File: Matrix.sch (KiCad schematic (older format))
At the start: 180 parts

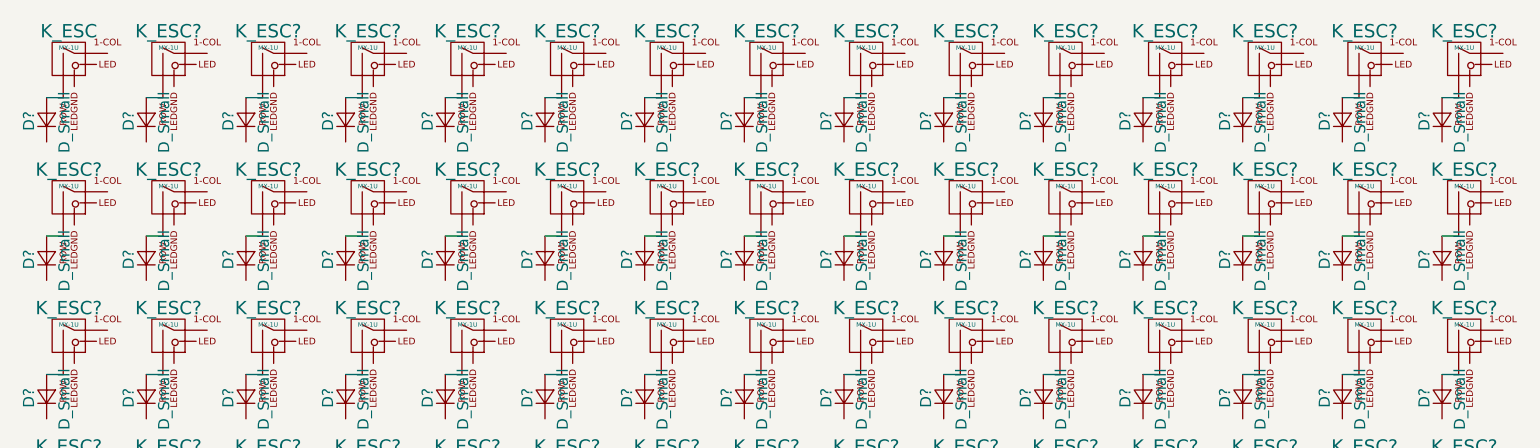
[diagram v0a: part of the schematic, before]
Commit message: Label row 1 of switches
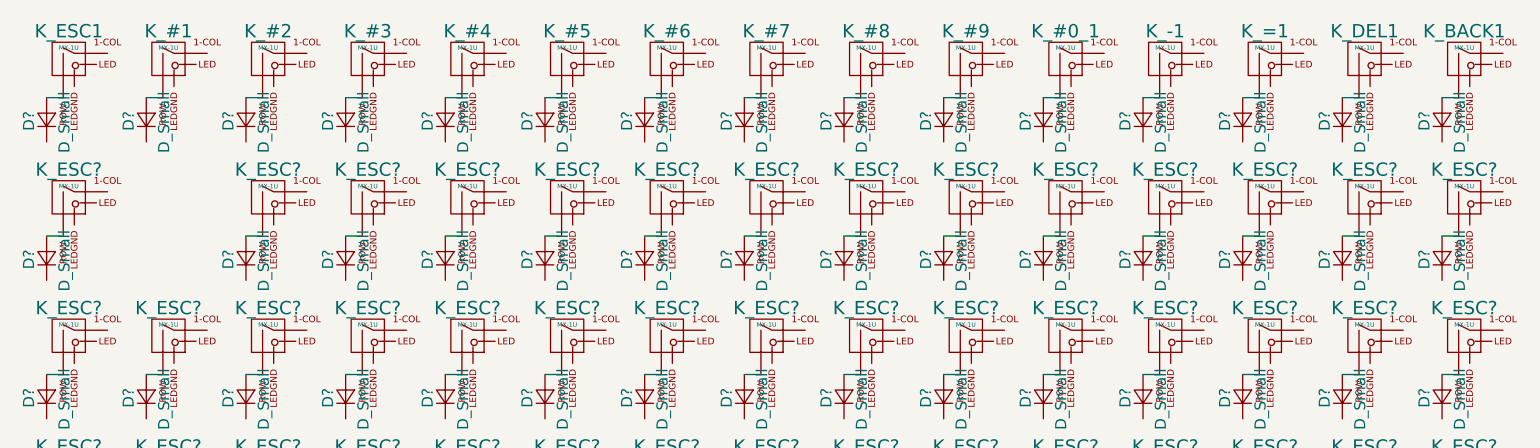
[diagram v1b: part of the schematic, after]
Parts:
- removed D?: D_Small, symbol D_Small
- removed K_ESC?: MX-1U, symbol MX-1U
- gave numbers to parts that had none: 14
- renumbered K_ESC to K_ESC1
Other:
- moved on the sheet: D?, K_#0_1, K_#1, K_#2, K_#3, K_#4, K_#5, K_#6, K_#7, K_#8, K_#9, K_-1
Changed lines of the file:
@@
 $EndDescr
 $Comp
-L MX-1U K_ESC
+L MX-1U K_ESC1
 U 1 1 5A641474
 P 1500 1225
-F 0 "K_ESC" H 1500 1350 60  0000 C CNN
+F 0 "K_ESC1" H 1500 1350 60  0000 C CNN
 F 1 "MX-1U" H 1500 1275 20  0000 C CNN
 F 2 "" H 1475 1200 60  0001 C CNN
@@
 	1475 1400 1400 1400
 $Comp
-L MX-1U K_ESC?
+L MX-1U K_-1
 U 1 1 5A646A8C
+P 6450 1225
+F 0 "K_-1" H 6450 1350 60  0000 C CNN
+F 1 "MX-1U" H 6450 1275 20  0000 C CNN
+F 2 "" H 6425 1200 60  0001 C CNN
+F 3 "" H 6425 1200 60  0001 C CNN
+	1    6450 1225
+	1    0    0    -1
+$EndComp
+$Comp
+L D_Small D?
+U 1 1 5A646A92
+P 6350 1500
+F 0 "D?" H 6300 1580 50  0000 L CNN
+F 1 "D_Small" H 6200 1420 50  0000 L CNN
+F 2 "" V 6350 1500 50  0001 C CNN
+F 3 "" V 6350 1500 50  0001 C CNN
+	1    6350 1500
+	0    -1   -1   0
+$EndComp
+Wire Wire Line
+	6425 1400 6350 1400
+$Comp
+L MX-1U K_#1
+U 1 1 5A646B3D
 P 1950 1225
-F 0 "K_ESC?" H 1950 1350 60  0000 C CNN
+F 0 "K_#1" H 1950 1350 60  0000 C CNN
 F 1 "MX-1U" H 1950 1275 20  0000 C CNN
 F 2 "" H 1925 1200 60  0001 C CNN
@@
 $Comp
 L D_Small D?
-U 1 1 5A646A92
+U 1 1 5A646B43
 P 1850 1500
 F 0 "D?" H 1800 1580 50  0000 L CNN
@@
 	1925 1400 1850 1400
 $Comp
-L MX-1U K_ESC?
-U 1 1 5A646B3D
+L MX-1U K_#2
+U 1 1 5A646B4A
 P 2400 1225
-F 0 "K_ESC?" H 2400 1350 60  0000 C CNN
+F 0 "K_#2" H 2400 1350 60  0000 C CNN
 F 1 "MX-1U" H 2400 1275 20  0000 C CNN
 F 2 "" H 2375 1200 60  0001 C CNN
@@
 $Comp
 L D_Small D?
-U 1 1 5A646B43
+U 1 1 5A646B50
 P 2300 1500
 F 0 "D?" H 2250 1580 50  0000 L CNN
@@
 	2375 1400 2300 1400
 $Comp
-L MX-1U K_ESC?
-U 1 1 5A646B4A
+L MX-1U K_#3
+U 1 1 5A646D37
 P 2850 1225
-F 0 "K_ESC?" H 2850 1350 60  0000 C CNN
+F 0 "K_#3" H 2850 1350 60  0000 C CNN
 F 1 "MX-1U" H 2850 1275 20  0000 C CNN
 F 2 "" H 2825 1200 60  0001 C CNN
@@
 $Comp
 L D_Small D?
-U 1 1 5A646B50
+U 1 1 5A646D3D
 P 2750 1500
 F 0 "D?" H 2700 1580 50  0000 L CNN
@@
 	2825 1400 2750 1400
 $Comp
-L MX-1U K_ESC?
-U 1 1 5A646D37
+L MX-1U K_#4
+U 1 1 5A646D44
 P 3300 1225
-F 0 "K_ESC?" H 3300 1350 60  0000 C CNN
+F 0 "K_#4" H 3300 1350 60  0000 C CNN
 F 1 "MX-1U" H 3300 1275 20  0000 C CNN
 F 2 "" H 3275 1200 60  0001 C CNN
@@
 $Comp
 L D_Small D?
-U 1 1 5A646D3D
+U 1 1 5A646D4A
 P 3200 1500
 F 0 "D?" H 3150 1580 50  0000 L CNN
@@
 	3275 1400 3200 1400
 $Comp
-L MX-1U K_ESC?
-U 1 1 5A646D44
+L MX-1U K_#5
+U 1 1 5A646D51
 P 3750 1225
-F 0 "K_ESC?" H 3750 1350 60  0000 C CNN
+F 0 "K_#5" H 3750 1350 60  0000 C CNN
 F 1 "MX-1U" H 3750 1275 20  0000 C CNN
 F 2 "" H 3725 1200 60  0001 C CNN
@@
 $Comp
 L D_Small D?
-U 1 1 5A646D4A
+U 1 1 5A646D57
 P 3650 1500
 F 0 "D?" H 3600 1580 50  0000 L CNN
@@
 	3725 1400 3650 1400
 $Comp
-L MX-1U K_ESC?
-U 1 1 5A646D51
+L MX-1U K_#6
+U 1 1 5A646D5E
 P 4200 1225
-F 0 "K_ESC?" H 4200 1350 60  0000 C CNN
+F 0 "K_#6" H 4200 1350 60  0000 C CNN
 F 1 "MX-1U" H 4200 1275 20  0000 C CNN
 F 2 "" H 4175 1200 60  0001 C CNN
@@
 $Comp
 L D_Small D?
-U 1 1 5A646D57
+U 1 1 5A646D64
 P 4100 1500
 F 0 "D?" H 4050 1580 50  0000 L CNN
@@
 	4175 1400 4100 1400
 $Comp
-L MX-1U K_ESC?
-U 1 1 5A646D5E
+L MX-1U K_#7
+U 1 1 5A64755B
 P 4650 1225
-F 0 "K_ESC?" H 4650 1350 60  0000 C CNN
+F 0 "K_#7" H 4650 1350 60  0000 C CNN
 F 1 "MX-1U" H 4650 1275 20  0000 C CNN
 F 2 "" H 4625 1200 60  0001 C CNN
@@
 $Comp
 L D_Small D?
-U 1 1 5A646D64
+U 1 1 5A647561
 P 4550 1500
 F 0 "D?" H 4500 1580 50  0000 L CNN
@@
 	4625 1400 4550 1400
 $Comp
-L MX-1U K_ESC?
-U 1 1 5A64755B
+L MX-1U K_#8
+U 1 1 5A647568
 P 5100 1225
-F 0 "K_ESC?" H 5100 1350 60  0000 C CNN
+F 0 "K_#8" H 5100 1350 60  0000 C CNN
 F 1 "MX-1U" H 5100 1275 20  0000 C CNN
 F 2 "" H 5075 1200 60  0001 C CNN
@@
 $Comp
 L D_Small D?
-U 1 1 5A647561
+U 1 1 5A64756E
 P 5000 1500
 F 0 "D?" H 4950 1580 50  0000 L CNN
@@
 	5075 1400 5000 1400
 $Comp
-L MX-1U K_ESC?
-U 1 1 5A647568
+L MX-1U K_#9
+U 1 1 5A647575
 P 5550 1225
-F 0 "K_ESC?" H 5550 1350 60  0000 C CNN
+F 0 "K_#9" H 5550 1350 60  0000 C CNN
 F 1 "MX-1U" H 5550 1275 20  0000 C CNN
 F 2 "" H 5525 1200 60  0001 C CNN
@@
 $Comp
 L D_Small D?
-U 1 1 5A64756E
+U 1 1 5A64757B
 P 5450 1500
 F 0 "D?" H 5400 1580 50  0000 L CNN
@@
 	5525 1400 5450 1400
 $Comp
-L MX-1U K_ESC?
-U 1 1 5A647575
+L MX-1U K_#0_1
+U 1 1 5A647582
 P 6000 1225
-F 0 "K_ESC?" H 6000 1350 60  0000 C CNN
+F 0 "K_#0_1" H 6000 1350 60  0000 C CNN
 F 1 "MX-1U" H 6000 1275 20  0000 C CNN
 F 2 "" H 5975 1200 60  0001 C CNN
@@
 $Comp
 L D_Small D?
-U 1 1 5A64757B
+U 1 1 5A647588
 P 5900 1500
 F 0 "D?" H 5850 1580 50  0000 L CNN
@@
 	5975 1400 5900 1400
 $Comp
-L MX-1U K_ESC?
-U 1 1 5A647582
-P 6450 1225
-F 0 "K_ESC?" H 6450 1350 60  0000 C CNN
-F 1 "MX-1U" H 6450 1275 20  0000 C CNN
-F 2 "" H 6425 1200 60  0001 C CNN
-F 3 "" H 6425 1200 60  0001 C CNN
-	1    6450 1225
-	1    0    0    -1
-$EndComp
-$Comp
-L D_Small D?
-U 1 1 5A647588
-P 6350 1500
-F 0 "D?" H 6300 1580 50  0000 L CNN
-F 1 "D_Small" H 6200 1420 50  0000 L CNN
-F 2 "" V 6350 1500 50  0001 C CNN
-F 3 "" V 6350 1500 50  0001 C CNN
-	1    6350 1500
-	0    -1   -1   0
-$EndComp
-Wire Wire Line
-	6425 1400 6350 1400
-$Comp
-L MX-1U K_ESC?
+L MX-1U K_=1
 U 1 1 5A64758F
 P 6900 1225
-F 0 "K_ESC?" H 6900 1350 60  0000 C CNN
+F 0 "K_=1" H 6900 1350 60  0000 C CNN
 F 1 "MX-1U" H 6900 1275 20  0000 C CNN
 F 2 "" H 6875 1200 60  0001 C CNN
@@
 	6875 1400 6800 1400
 $Comp
-L MX-1U K_ESC?
+L MX-1U K_DEL1
 U 1 1 5A64759C
 P 7350 1225
-F 0 "K_ESC?" H 7350 1350 60  0000 C CNN
+F 0 "K_DEL1" H 7350 1350 60  0000 C CNN
 F 1 "MX-1U" H 7350 1275 20  0000 C CNN
 F 2 "" H 7325 1200 60  0001 C CNN
@@
 	7325 1400 7250 1400
 $Comp
-L MX-1U K_ESC?
+L MX-1U K_BACK1
 U 1 1 5A6475A9
 P 7800 1225
-F 0 "K_ESC?" H 7800 1350 60  0000 C CNN
+F 0 "K_BACK1" H 7800 1350 60  0000 C CNN
 F 1 "MX-1U" H 7800 1275 20  0000 C CNN
 F 2 "" H 7775 1200 60  0001 C CNN
@@
 $Comp
 L MX-1U K_ESC?
-U 1 1 5A647EB5
-P 1950 1850
-F 0 "K_ESC?" H 1950 1975 60  0000 C CNN
-F 1 "MX-1U" H 1950 1900 20  0000 C CNN
-F 2 "" H 1925 1825 60  0001 C CNN
-F 3 "" H 1925 1825 60  0001 C CNN
-	1    1950 1850
-	1    0    0    -1
-$EndComp
-$Comp
-L D_Small D?
-U 1 1 5A647EBB
-P 1850 2125
-F 0 "D?" H 1800 2205 50  0000 L CNN
-F 1 "D_Small" H 1700 2045 50  0000 L CNN
-F 2 "" V 1850 2125 50  0001 C CNN
-F 3 "" V 1850 2125 50  0001 C CNN
-	1    1850 2125
-	0    -1   -1   0
-$EndComp
-Wire Wire Line
-	1925 2025 1850 2025
-$Comp
-L MX-1U K_ESC?

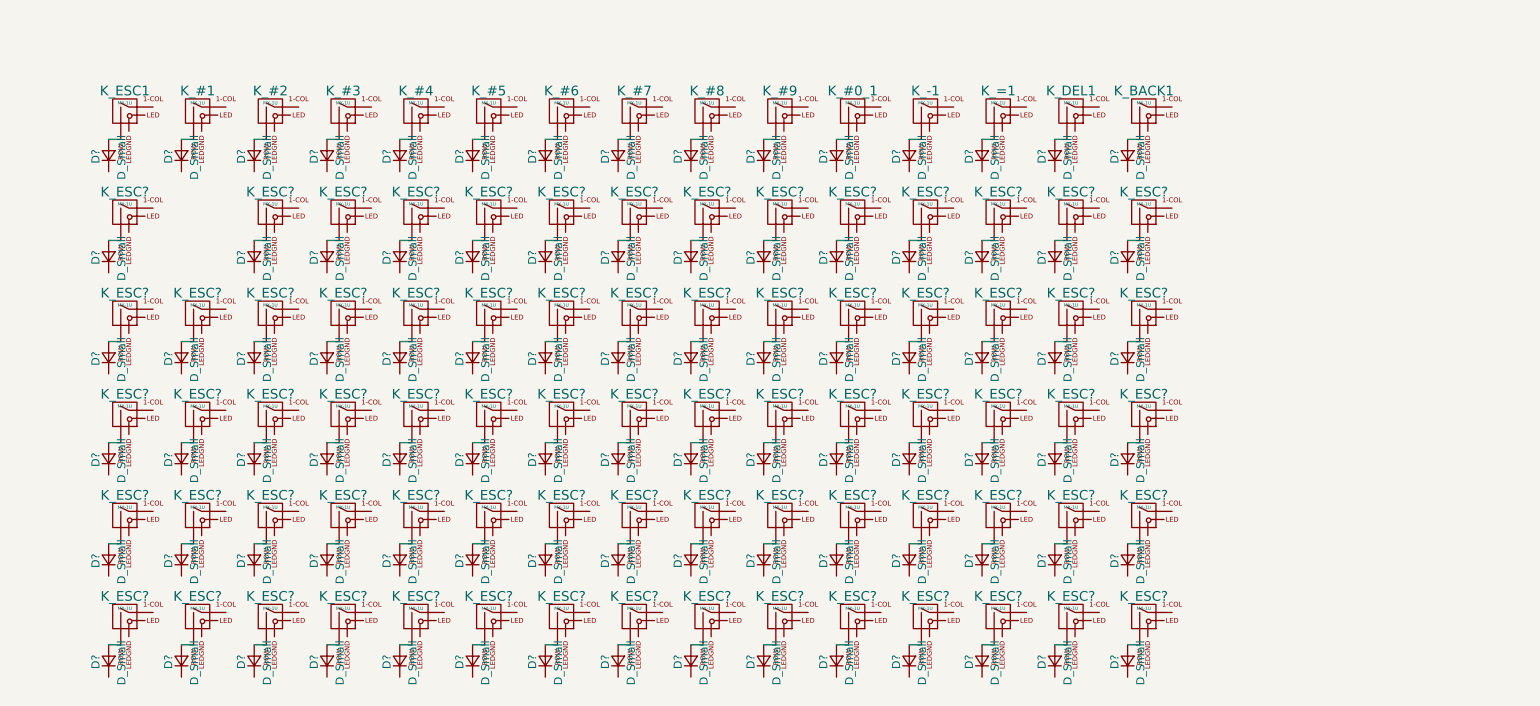
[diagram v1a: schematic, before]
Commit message: Continue labeling and adding keys on matrix
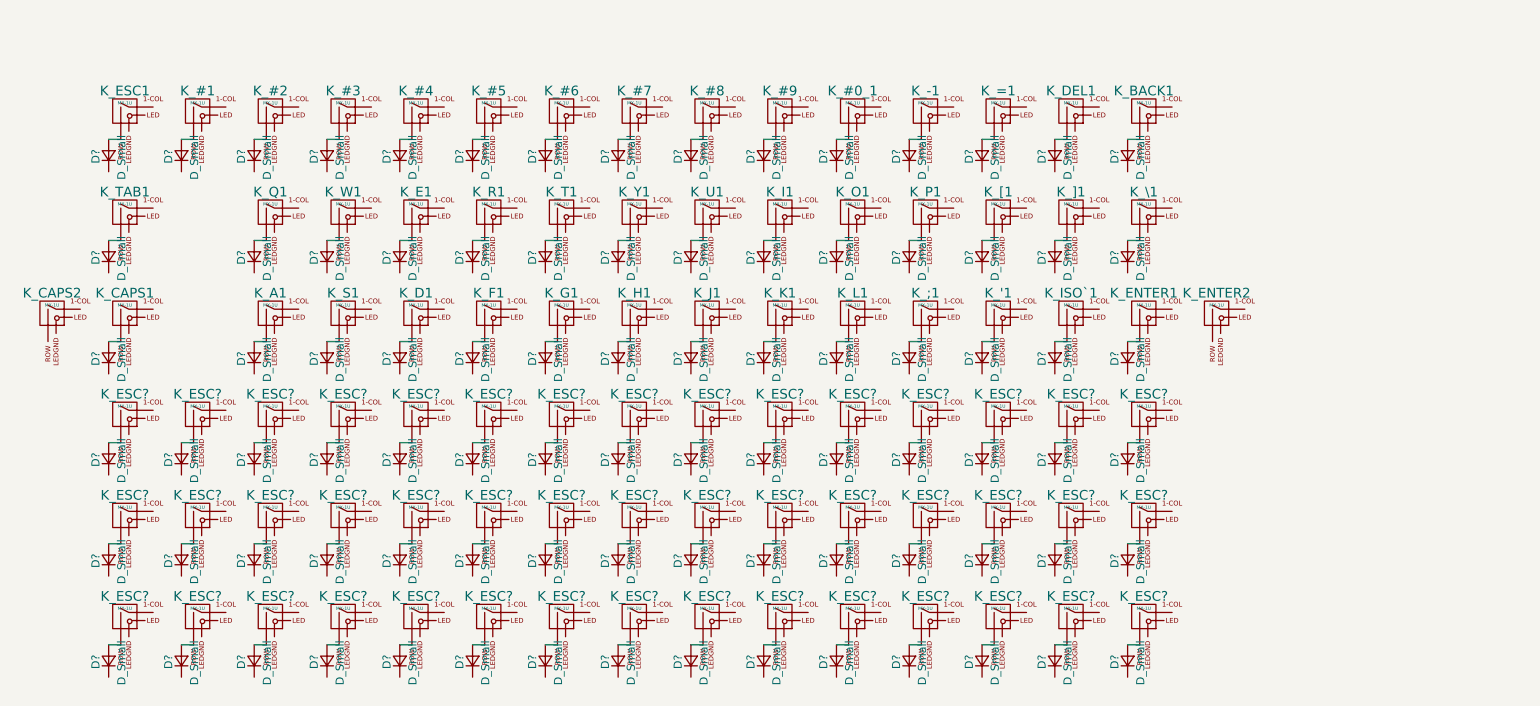
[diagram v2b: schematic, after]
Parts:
- removed D?: D_Small, symbol D_Small
- removed K_ESC?: MX-1U, symbol MX-1U
- added K_CAPS2, K_ENTER2: MX-1U, symbol MX-1U
- gave numbers to parts that had none: 28
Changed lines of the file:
@@
 	7775 1400 7700 1400
 $Comp
-L MX-1U K_ESC?
+L MX-1U K_TAB1
 U 1 1 5A647EA8
 P 1500 1850
-F 0 "K_ESC?" H 1500 1975 60  0000 C CNN
+F 0 "K_TAB1" H 1500 1975 60  0000 C CNN
 F 1 "MX-1U" H 1500 1900 20  0000 C CNN
 F 2 "" H 1475 1825 60  0001 C CNN
@@
 	1475 2025 1400 2025
 $Comp
-L MX-1U K_ESC?
+L MX-1U K_Q1
 U 1 1 5A647EC2
 P 2400 1850
-F 0 "K_ESC?" H 2400 1975 60  0000 C CNN
+F 0 "K_Q1" H 2400 1975 60  0000 C CNN
 F 1 "MX-1U" H 2400 1900 20  0000 C CNN
 F 2 "" H 2375 1825 60  0001 C CNN
@@
 	2375 2025 2300 2025
 $Comp
-L MX-1U K_ESC?
+L MX-1U K_W1
 U 1 1 5A647ECF
 P 2850 1850
-F 0 "K_ESC?" H 2850 1975 60  0000 C CNN
+F 0 "K_W1" H 2850 1975 60  0000 C CNN
 F 1 "MX-1U" H 2850 1900 20  0000 C CNN
 F 2 "" H 2825 1825 60  0001 C CNN
@@
 	2825 2025 2750 2025
 $Comp
-L MX-1U K_ESC?
+L MX-1U K_E1
 U 1 1 5A647EDC
 P 3300 1850
-F 0 "K_ESC?" H 3300 1975 60  0000 C CNN
+F 0 "K_E1" H 3300 1975 60  0000 C CNN
 F 1 "MX-1U" H 3300 1900 20  0000 C CNN
 F 2 "" H 3275 1825 60  0001 C CNN
@@
 	3275 2025 3200 2025
 $Comp
-L MX-1U K_ESC?
+L MX-1U K_R1
 U 1 1 5A647EE9
 P 3750 1850
-F 0 "K_ESC?" H 3750 1975 60  0000 C CNN
+F 0 "K_R1" H 3750 1975 60  0000 C CNN
 F 1 "MX-1U" H 3750 1900 20  0000 C CNN
 F 2 "" H 3725 1825 60  0001 C CNN
@@
 	3725 2025 3650 2025
 $Comp
-L MX-1U K_ESC?
+L MX-1U K_T1
 U 1 1 5A647EF6
 P 4200 1850
-F 0 "K_ESC?" H 4200 1975 60  0000 C CNN
+F 0 "K_T1" H 4200 1975 60  0000 C CNN
 F 1 "MX-1U" H 4200 1900 20  0000 C CNN
 F 2 "" H 4175 1825 60  0001 C CNN
@@
 	4175 2025 4100 2025
 $Comp
-L MX-1U K_ESC?
+L MX-1U K_Y1
 U 1 1 5A647F03
 P 4650 1850
-F 0 "K_ESC?" H 4650 1975 60  0000 C CNN
+F 0 "K_Y1" H 4650 1975 60  0000 C CNN
 F 1 "MX-1U" H 4650 1900 20  0000 C CNN
 F 2 "" H 4625 1825 60  0001 C CNN
@@
 	4625 2025 4550 2025
 $Comp
-L MX-1U K_ESC?
+L MX-1U K_U1
 U 1 1 5A647F10
 P 5100 1850
-F 0 "K_ESC?" H 5100 1975 60  0000 C CNN
+F 0 "K_U1" H 5100 1975 60  0000 C CNN
 F 1 "MX-1U" H 5100 1900 20  0000 C CNN
 F 2 "" H 5075 1825 60  0001 C CNN
@@
 	5075 2025 5000 2025
 $Comp
-L MX-1U K_ESC?
+L MX-1U K_I1
 U 1 1 5A647F1D
 P 5550 1850
-F 0 "K_ESC?" H 5550 1975 60  0000 C CNN
+F 0 "K_I1" H 5550 1975 60  0000 C CNN
 F 1 "MX-1U" H 5550 1900 20  0000 C CNN
 F 2 "" H 5525 1825 60  0001 C CNN
@@
 	5525 2025 5450 2025
 $Comp
-L MX-1U K_ESC?
+L MX-1U K_O1
 U 1 1 5A647F2A
 P 6000 1850
-F 0 "K_ESC?" H 6000 1975 60  0000 C CNN
+F 0 "K_O1" H 6000 1975 60  0000 C CNN
 F 1 "MX-1U" H 6000 1900 20  0000 C CNN
 F 2 "" H 5975 1825 60  0001 C CNN
@@
 	5975 2025 5900 2025
 $Comp
-L MX-1U K_ESC?
+L MX-1U K_P1
 U 1 1 5A647F37
 P 6450 1850
-F 0 "K_ESC?" H 6450 1975 60  0000 C CNN
+F 0 "K_P1" H 6450 1975 60  0000 C CNN
 F 1 "MX-1U" H 6450 1900 20  0000 C CNN
 F 2 "" H 6425 1825 60  0001 C CNN
@@
 	6425 2025 6350 2025
 $Comp
-L MX-1U K_ESC?
+L MX-1U K_[1
 U 1 1 5A647F44
 P 6900 1850
-F 0 "K_ESC?" H 6900 1975 60  0000 C CNN
+F 0 "K_[1" H 6900 1975 60  0000 C CNN
 F 1 "MX-1U" H 6900 1900 20  0000 C CNN
 F 2 "" H 6875 1825 60  0001 C CNN
@@
 	6875 2025 6800 2025
 $Comp
-L MX-1U K_ESC?
+L MX-1U K_]1
 U 1 1 5A647F51
 P 7350 1850
-F 0 "K_ESC?" H 7350 1975 60  0000 C CNN
+F 0 "K_]1" H 7350 1975 60  0000 C CNN
 F 1 "MX-1U" H 7350 1900 20  0000 C CNN
 F 2 "" H 7325 1825 60  0001 C CNN
@@
 	7325 2025 7250 2025
 $Comp
-L MX-1U K_ESC?
+L MX-1U K_\1
 U 1 1 5A647F5E
 P 7800 1850
-F 0 "K_ESC?" H 7800 1975 60  0000 C CNN
+F 0 "K_\\1" H 7800 1975 60  0000 C CNN
 F 1 "MX-1U" H 7800 1900 20  0000 C CNN
 F 2 "" H 7775 1825 60  0001 C CNN
@@
 	7775 2025 7700 2025
 $Comp
-L MX-1U K_ESC?
+L MX-1U K_CAPS1
 U 1 1 5A6497CC
 P 1500 2475
-F 0 "K_ESC?" H 1500 2600 60  0000 C CNN
+F 0 "K_CAPS1" H 1500 2600 60  0000 C CNN
 F 1 "MX-1U" H 1500 2525 20  0000 C CNN
 F 2 "" H 1475 2450 60  0001 C CNN
@@
 	1475 2650 1400 2650
 $Comp
-L MX-1U K_ESC?
-U 1 1 5A6497D9
-P 1950 2475
-F 0 "K_ESC?" H 1950 2600 60  0000 C CNN
-F 1 "MX-1U" H 1950 2525 20  0000 C CNN
-F 2 "" H 1925 2450 60  0001 C CNN
-F 3 "" H 1925 2450 60  0001 C CNN
-	1    1950 2475
-	1    0    0    -1
-$EndComp
-$Comp
-L D_Small D?
-U 1 1 5A6497DF
-P 1850 2750
-F 0 "D?" H 1800 2830 50  0000 L CNN
-F 1 "D_Small" H 1700 2670 50  0000 L CNN
-F 2 "" V 1850 2750 50  0001 C CNN
-F 3 "" V 1850 2750 50  0001 C CNN
-	1    1850 2750
-	0    -1   -1   0
-$EndComp
-Wire Wire Line
-	1925 2650 1850 2650
-$Comp
-L MX-1U K_ESC?
+L MX-1U K_A1
 U 1 1 5A6497E6
 P 2400 2475
-F 0 "K_ESC?" H 2400 2600 60  0000 C CNN
+F 0 "K_A1" H 2400 2600 60  0000 C CNN
 F 1 "MX-1U" H 2400 2525 20  0000 C CNN
 F 2 "" H 2375 2450 60  0001 C CNN
@@
 	2375 2650 2300 2650
 $Comp
-L MX-1U K_ESC?
+L MX-1U K_S1
 U 1 1 5A6497F3
 P 2850 2475
-F 0 "K_ESC?" H 2850 2600 60  0000 C CNN
+F 0 "K_S1" H 2850 2600 60  0000 C CNN
 F 1 "MX-1U" H 2850 2525 20  0000 C CNN
 F 2 "" H 2825 2450 60  0001 C CNN
@@
 	2825 2650 2750 2650
 $Comp
-L MX-1U K_ESC?
+L MX-1U K_D1
 U 1 1 5A649800
 P 3300 2475
-F 0 "K_ESC?" H 3300 2600 60  0000 C CNN
+F 0 "K_D1" H 3300 2600 60  0000 C CNN
 F 1 "MX-1U" H 3300 2525 20  0000 C CNN
 F 2 "" H 3275 2450 60  0001 C CNN
@@
 	3275 2650 3200 2650
 $Comp
-L MX-1U K_ESC?
+L MX-1U K_F1
 U 1 1 5A64980D
 P 3750 2475
-F 0 "K_ESC?" H 3750 2600 60  0000 C CNN
+F 0 "K_F1" H 3750 2600 60  0000 C CNN
 F 1 "MX-1U" H 3750 2525 20  0000 C CNN
 F 2 "" H 3725 2450 60  0001 C CNN
@@
 	3725 2650 3650 2650
 $Comp
-L MX-1U K_ESC?
+L MX-1U K_G1
 U 1 1 5A64981A
 P 4200 2475
-F 0 "K_ESC?" H 4200 2600 60  0000 C CNN
+F 0 "K_G1" H 4200 2600 60  0000 C CNN
 F 1 "MX-1U" H 4200 2525 20  0000 C CNN
 F 2 "" H 4175 2450 60  0001 C CNN
@@
 	4175 2650 4100 2650
 $Comp
-L MX-1U K_ESC?
+L MX-1U K_H1
 U 1 1 5A649827
 P 4650 2475
-F 0 "K_ESC?" H 4650 2600 60  0000 C CNN
+F 0 "K_H1" H 4650 2600 60  0000 C CNN
 F 1 "MX-1U" H 4650 2525 20  0000 C CNN
 F 2 "" H 4625 2450 60  0001 C CNN
@@
 	4625 2650 4550 2650
 $Comp
-L MX-1U K_ESC?
+L MX-1U K_J1
 U 1 1 5A649834
 P 5100 2475
-F 0 "K_ESC?" H 5100 2600 60  0000 C CNN
+F 0 "K_J1" H 5100 2600 60  0000 C CNN
 F 1 "MX-1U" H 5100 2525 20  0000 C CNN
 F 2 "" H 5075 2450 60  0001 C CNN
@@
 	5075 2650 5000 2650
 $Comp
-L MX-1U K_ESC?
+L MX-1U K_K1
 U 1 1 5A649841
 P 5550 2475
-F 0 "K_ESC?" H 5550 2600 60  0000 C CNN
+F 0 "K_K1" H 5550 2600 60  0000 C CNN
 F 1 "MX-1U" H 5550 2525 20  0000 C CNN
 F 2 "" H 5525 2450 60  0001 C CNN
@@
 	5525 2650 5450 2650
 $Comp
-L MX-1U K_ESC?
+L MX-1U K_L1
 U 1 1 5A64984E
 P 6000 2475
-F 0 "K_ESC?" H 6000 2600 60  0000 C CNN
+F 0 "K_L1" H 6000 2600 60  0000 C CNN
 F 1 "MX-1U" H 6000 2525 20  0000 C CNN
 F 2 "" H 5975 2450 60  0001 C CNN
@@
 	5975 2650 5900 2650
 $Comp
-L MX-1U K_ESC?
+L MX-1U K_;1
 U 1 1 5A64985B
 P 6450 2475
-F 0 "K_ESC?" H 6450 2600 60  0000 C CNN
+F 0 "K_;1" H 6450 2600 60  0000 C CNN
 F 1 "MX-1U" H 6450 2525 20  0000 C CNN
 F 2 "" H 6425 2450 60  0001 C CNN
@@
 	6425 2650 6350 2650
 $Comp
-L MX-1U K_ESC?
+L MX-1U K_'1
 U 1 1 5A649868
 P 6900 2475
-F 0 "K_ESC?" H 6900 2600 60  0000 C CNN
+F 0 "K_'1" H 6900 2600 60  0000 C CNN
 F 1 "MX-1U" H 6900 2525 20  0000 C CNN
 F 2 "" H 6875 2450 60  0001 C CNN
@@
 	6875 2650 6800 2650
 $Comp
-L MX-1U K_ESC?
+L MX-1U K_ISO`1
 U 1 1 5A649875
 P 7350 2475
-F 0 "K_ESC?" H 7350 2600 60  0000 C CNN
+F 0 "K_ISO`1" H 7350 2600 60  0000 C CNN
 F 1 "MX-1U" H 7350 2525 20  0000 C CNN
 F 2 "" H 7325 2450 60  0001 C CNN
@@
 	7325 2650 7250 2650
 $Comp
-L MX-1U K_ESC?
+L MX-1U K_ENTER1
 U 1 1 5A649882
 P 7800 2475
-F 0 "K_ESC?" H 7800 2600 60  0000 C CNN
+F 0 "K_ENTER1" H 7800 2600 60  0000 C CNN
 F 1 "MX-1U" H 7800 2525 20  0000 C CNN
 F 2 "" H 7775 2450 60  0001 C CNN
@@
 Wire Wire Line
 	7775 4525 7700 4525
+$Comp
+L MX-1U K_CAPS2
+U 1 1 5A660657
+P 1050 2475
+F 0 "K_CAPS2" H 1050 2600 60  0000 C CNN
+F 1 "MX-1U" H 1050 2525 20  0000 C CNN
+F 2 "" H 1025 2450 60  0001 C CNN
+F 3 "" H 1025 2450 60  0001 C CNN
+	1    1050 2475
+	1    0    0    -1
+$EndComp
+$Comp
+L MX-1U K_ENTER2
+U 1 1 5A6653CE
+P 8250 2475
+F 0 "K_ENTER2" H 8250 2600 60  0000 C CNN
+F 1 "MX-1U" H 8250 2525 20  0000 C CNN
+F 2 "" H 8225 2450 60  0001 C CNN
+F 3 "" H 8225 2450 60  0001 C CNN
+	1    8250 2475
+	1    0    0    -1
+$EndComp
 $EndSCHEMATC
